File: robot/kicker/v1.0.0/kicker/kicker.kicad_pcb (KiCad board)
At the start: 2 copper layers, 0 parts

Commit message: first layout
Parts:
- added C1: 22u 25V, Capacitor_SMD:C_1210_3225Metric, F.Cu at (161.2, 130.9)
- added C10: 1000uF 200V, AT-Capacitors:ESMQ201VSN102MQ35S, F.Cu at (248.0, 177.0)
- added C11: 0.1u, Capacitor_SMD:C_0603_1608Metric, F.Cu at (427.7, 50.1)
- added C12: 0.1u, Capacitor_SMD:C_0603_1608Metric, F.Cu at (97.0, 99.5)
- added C13: 330u 50V, AT-Capacitors:WE-860160675028, F.Cu at (181.6, 164.3)
- added C14: 10u 50V, Capacitor_SMD:C_1210_3225Metric, F.Cu at (209.8, 175.6)
- added C15: 10u 35V, Capacitor_SMD:C_1206_3216Metric, B.Cu at (217.9, 129.9)
- added C16: 0.1u, Capacitor_SMD:C_0603_1608Metric, F.Cu at (371.4, 123.2)
- added C17: 10u 50V, Capacitor_SMD:C_1210_3225Metric, F.Cu at (213.3, 175.6)
- added C18: 0.1u, Capacitor_SMD:C_0603_1608Metric, F.Cu at (363.4, 126.1)
- added C19: 0.1u, Capacitor_SMD:C_0603_1608Metric, F.Cu at (218.0, 128.5)
- added C2: 47u 10V, Capacitor_SMD:C_1210_3225Metric, F.Cu at (77.6, 108.1)
- added C20: 10u 50V, Capacitor_SMD:C_1210_3225Metric, F.Cu at (216.8, 175.6)
- added C21: 10u 50V, Capacitor_SMD:C_1210_3225Metric, F.Cu at (220.3, 175.6)
- added C22: 0.1u 200V, Capacitor_SMD:C_1206_3216Metric, F.Cu at (208.9, 130.1)
- added C23: 10u 50v, Capacitor_SMD:C_1210_3225Metric, F.Cu at (449.5, 77.2)
- added C24: 0.1u, Capacitor_SMD:C_0603_1608Metric, F.Cu at (470.4, 71.1)
- added C25: DNP, Capacitor_SMD:C_0603_1608Metric, F.Cu at (470.4, 68.6)
- added C26: DNP, Capacitor_SMD:C_0603_1608Metric, F.Cu at (462.4, 76.3)
- added C27: 4u7 25V, Capacitor_SMD:C_0805_2012Metric, F.Cu at (119.1, 54.1)
- added C28: 0.1u, Capacitor_SMD:C_0603_1608Metric, F.Cu at (105.0, 71.9)
- added C29: 0.1u, Capacitor_SMD:C_0603_1608Metric, F.Cu at (111.0, 64.0)
- added C3: 1u 10V, Capacitor_SMD:C_0603_1608Metric, F.Cu at (106.4, 94.1)
- added C30: 10n 10V, Capacitor_SMD:C_0603_1608Metric, F.Cu at (126.1, 50.0)
- added C31: 1u 10V, Capacitor_SMD:C_0603_1608Metric, F.Cu at (97.0, 79.5)
- added C32: 4u7 25V, Capacitor_SMD:C_0805_2012Metric, F.Cu at (106.3, 66.6)
- added C4: 47u 10V, Capacitor_SMD:C_1210_3225Metric, F.Cu at (155.6, 130.9)
- added C5: 1u 10V, Capacitor_SMD:C_0603_1608Metric, F.Cu at (86.6, 112.3)
- added C6: 1000uF 200V, AT-Capacitors:ESMQ201VSN102MQ35S, F.Cu at (248.0, 122.8)
- added C7: 0.1u, Capacitor_SMD:C_0603_1608Metric, F.Cu at (101.0, 99.5)
- added C8: 1000uF 200V, AT-Capacitors:ESMQ201VSN102MQ35S, F.Cu at (248.0, 149.9)
- added C9: 0.1u, Capacitor_SMD:C_0603_1608Metric, F.Cu at (434.5, 41.3)
- added D1: Green, AT-LED:LED0603, F.Cu at (69.8, 112.0)
- added D10: FR3G_R1_00001, Diode_SMD:D_SMC, F.Cu at (237.0, 112.0)
- added D11: FR3G_R1_00001, Diode_SMD:D_SMC, F.Cu at (237.7, 187.3)
- added D12: Blue, AT-LED:LED0603, F.Cu at (111.0, 61.5)
- added D13: Green, AT-LED:LED0603, F.Cu at (130.3, 42.5)
- added D14: Red, AT-LED:LED0603, F.Cu at (97.0, 77.0)
- added D2: MURS460, Diode_SMD:D_SMC, F.Cu at (91.0, 94.2)
- added D3: Green, AT-LED:LED0603, F.Cu at (78.5, 111.5)
- added D4: 824521261, AT-Discrete:D_SMB_Non-Polar, F.Cu at (148.6, 131.3)
- added D5: MURS460, Diode_SMD:D_SMC, F.Cu at (427.1, 41.4)
- added D6: Green, AT-LED:LED0603, F.Cu at (82.6, 110.8)
- added D7: 824540121, Diode_SMD:D_SMC, F.Cu at (79.2, 91.7)
- added D8: RED, AT-LED:LED0603, F.Cu at (434.5, 38.8)
- added D9: MURS460, Diode_SMD:D_SMC, F.Cu at (236.5, 167.5)
- added F1: 40A, AT-Fuses:3557-2, F.Cu at (199.2, 171.5)
- added F2: 1.5A Fast Blow, Fuse:Fuse_0603_1608Metric, F.Cu at (106.4, 91.5)
- added F3: 1.5A Fast Blow, Fuse:Fuse_0603_1608Metric, F.Cu at (90.8, 107.2)
- added H1: M3, MountingHole:MountingHole_3.2mm_M3, F.Cu at (182.5, 177.5)
- added H2: M3, MountingHole:MountingHole_3.2mm_M3, F.Cu at (237.5, 177.5)
- added H3: M3, MountingHole:MountingHole_3.2mm_M3, F.Cu at (182.5, 122.5)
- added H4: M3, MountingHole:MountingHole_3.2mm_M3, F.Cu at (237.5, 122.5)
- added J1: XT30PW-M, Connector_AMASS:AMASS_XT30PW-M_1x02_P2.50mm_Horizontal, F.Cu at (192.5, 184.8)
- added J2: 1054052108, AT-Connectors:1054052108, F.Cu at (195.0, 106.5)
- added J3: 2157601002, AT-Connectors:2157601002, F.Cu at (243.5, 103.0)
- added J4: 2157601002, AT-Connectors:2157601002, F.Cu at (243.7, 196.0)
- added J5: Conn_ARM_JTAG_SWD_10, AT-Connectors:Samtec-2x5pin-0.5mm, F.Cu at (99.0, 71.7)
- added J6: Conn_01x03, Connector_PinSocket_2.54mm:PinSocket_1x03_P2.54mm_Horizontal, F.Cu at (185.9, 191.5)
- added J7: Conn_01x03, Connector_PinSocket_2.54mm:PinSocket_1x03_P2.54mm_Horizontal, F.Cu at (186.4, 128.5)
- added JP1: Power Iso., Jumper:SolderJumper-2_P1.3mm_Bridged_RoundedPad1.0x1.5mm, F.Cu at (423.8, 47.0)
- added JP2: Charge Bypass Jumper, Jumper:SolderJumper-2_P1.3mm_Open_RoundedPad1.0x1.5mm, F.Cu at (74.3, 112.0)
- added JP3: Kick Bypass Jumper, Jumper:SolderJumper-2_P1.3mm_Open_RoundedPad1.0x1.5mm, F.Cu at (92.8, 99.8)
- added JP4: Chip Bypass Jumper, Jumper:SolderJumper-2_P1.3mm_Open_RoundedPad1.0x1.5mm, F.Cu at (82.6, 107.8)
- added JP5: Fault Bypass Jumper, Jumper:SolderJumper-2_P1.3mm_Open_RoundedPad1.0x1.5mm, F.Cu at (70.0, 109.0)
- added JP6: SolderJumper_2_Bridged, Jumper:SolderJumper-2_P1.3mm_Bridged_RoundedPad1.0x1.5mm, F.Cu at (215.5, 123.0)
- added JP7: Disable Micro, Jumper:SolderJumper-2_P1.3mm_Open_RoundedPad1.0x1.5mm, F.Cu at (121.9, 50.6)
- added L1: 650 @100MHz, Resistor_SMD:R_0603_1608Metric, F.Cu at (367.8, 115.7)
- added L2: 650 @100MHz, Resistor_SMD:R_0603_1608Metric, F.Cu at (371.8, 115.7)
- added L3: GA3460-BL, AT-Inductors:GA34XX-BL, F.Cu at (219.5, 152.0)
- added L4: 650 @100MHz, Resistor_SMD:R_0603_1608Metric, F.Cu at (115.0, 61.5)
- added Q1: BSC0402NSATMA1, Package_TO_SOT_SMD:TDSON-8-1, F.Cu at (213.0, 130.5)
- added Q2: IXXH110N65C4, Package_TO_SOT_THT:TO-247-3_Horizontal_TabDown, F.Cu at (229.4, 113.0)
- added Q3: IXXH110N65C4, Package_TO_SOT_THT:TO-247-3_Horizontal_TabDown, F.Cu at (230.6, 196.7)
- added Q4: BSS138K, Package_TO_SOT_SMD:SOT-23, F.Cu at (106.5, 62.9)
- added R1: 22k, Resistor_SMD:R_0603_1608Metric, F.Cu at (416.5, 62.4)
- added R10: 1M47, Resistor_SMD:R_0603_1608Metric, F.Cu at (428.0, 46.5)
- added R11: 15k, Resistor_SMD:R_0603_1608Metric, F.Cu at (97.0, 102.0)
- added R12: 100k, Resistor_SMD:R_0603_1608Metric, F.Cu at (367.4, 123.2)
- added R13: 100k, Resistor_SMD:R_0603_1608Metric, F.Cu at (375.8, 116.0)
- added R14: 100k, Resistor_SMD:R_0603_1608Metric, F.Cu at (375.4, 123.6)
- added R15: 316k 1%, Resistor_SMD:R_0603_1608Metric, F.Cu at (379.5, 121.1)
- added R16: 523k 1%, Resistor_SMD:R_0603_1608Metric, F.Cu at (371.4, 125.7)
- added R17: 205k 1%, Resistor_SMD:R_0603_1608Metric, F.Cu at (375.4, 121.1)
- added R18: 226k 1%, Resistor_SMD:R_0603_1608Metric, F.Cu at (379.8, 116.0)
- added R19: 36k5 1%, Resistor_SMD:R_0603_1608Metric, F.Cu at (225.3, 123.1)
- added R2: 10k, Resistor_SMD:R_0603_1608Metric, F.Cu at (423.7, 52.6)
- added R20: 1 1%, Resistor_SMD:R_0603_1608Metric, F.Cu at (208.5, 126.2)
- added R21: 4k21, Resistor_SMD:R_0603_1608Metric, F.Cu at (218.0, 130.0)
- added R22: 36k5 1%, Resistor_SMD:R_0603_1608Metric, F.Cu at (222.0, 132.5)
- added R23: 80k6 1%, Resistor_SMD:R_0603_1608Metric, F.Cu at (220.5, 132.5)
- added R24: 3m00 1% 1W, AT-Resistors:1206-CS, F.Cu at (214.2, 125.5)
- added R25: 237k 1%, Resistor_SMD:R_0603_1608Metric, B.Cu at (230.5, 126.0)
- added R26: 237k 1%, Resistor_SMD:R_0603_1608Metric, B.Cu at (230.5, 122.5)
- added R27: 2k94 1%, Resistor_SMD:R_0603_1608Metric, B.Cu at (230.5, 118.0)
- added R28: 100k, Resistor_SMD:R_0603_1608Metric, F.Cu at (454.4, 76.3)
- added R29: 100k, Resistor_SMD:R_0603_1608Metric, F.Cu at (474.4, 68.6)
- added R3: 267k, Resistor_SMD:R_0603_1608Metric, F.Cu at (438.6, 38.8)
- added R30: 100k, Resistor_SMD:R_0603_1608Metric, F.Cu at (458.4, 76.3)
- added R31: 100k, Resistor_SMD:R_0603_1608Metric, F.Cu at (483.6, 58.1)
- added R32: 10, Resistor_SMD:R_0603_1608Metric, F.Cu at (483.6, 55.6)
- added R33: 10, Resistor_SMD:R_0603_1608Metric, F.Cu at (492.1, 49.1)
- added R34: 100k, Resistor_SMD:R_0603_1608Metric, F.Cu at (118.9, 56.9)
- added R35: 10k, Resistor_SMD:R_0603_1608Metric, F.Cu at (105.0, 69.3)
- added R36: 10k, Resistor_SMD:R_0603_1608Metric, F.Cu at (130.3, 45.0)
- added R37: 10k, Resistor_SMD:R_0603_1608Metric, F.Cu at (123.4, 53.6)
- added R4: 18k7, Resistor_SMD:R_0603_1608Metric, F.Cu at (92.6, 102.8)
- added R5: 10k, Resistor_SMD:R_0603_1608Metric, F.Cu at (408.5, 70.3)
- added R6: 510k, Resistor_SMD:R_0603_1608Metric, F.Cu at (86.7, 107.2)
- added R7: 510k, Resistor_SMD:R_0603_1608Metric, F.Cu at (86.7, 109.8)
- added R8: 15k, Resistor_SMD:R_0603_1608Metric, F.Cu at (432.0, 46.5)
- added R9: 1M47, Resistor_SMD:R_0603_1608Metric, F.Cu at (423.7, 50.1)
- added SW1: TS02-66-73-BK-160-SCR-D, at-switches:TS02-66-73-BK-160-SCR-D, F.Cu at (99.6, 64.2)
- added TP1: ~{DONE}, TestPoint:TestPoint_Pad_D1.5mm, F.Cu at (375.1, 128.8)
- added TP2: CHG_EN, TestPoint:TestPoint_Pad_D1.5mm, F.Cu at (363.2, 134.8)
- added TP3: ~{FAULT}, TestPoint:TestPoint_Pad_D1.5mm, F.Cu at (366.7, 134.8)
- added TP5: SPICE: V_{drain} <<<HIGH VOLTAGE>>>, TestPoint:TestPoint_Pad_D1.0mm, F.Cu at (209.0, 133.5)
- added TP6: SPICE: V_{out} <<<HIGH VOLTAGE>>>, TestPoint:TestPoint_Pad_D1.5mm, F.Cu at (240.2, 162.0)
- added TP7: FB, TestPoint:TestPoint_Pad_D1.5mm, B.Cu at (229.0, 130.5)
- added U1: LM1117-5.0, Package_TO_SOT_SMD:TO-252-2, F.Cu at (150.5, 124.5)
- added U2: LM1117-3.3, Package_TO_SOT_SMD:SOT-223-3_TabPin2, F.Cu at (161.5, 124.7)
- added U3: ADUM7441, Package_SO:QSOP-16_3.9x4.9mm_P0.635mm, F.Cu at (195.0, 126.0)
- added U4: LT3751-QFN, AT-IC:LT3751-QFN20_EP_4x5mm_P0.5mm, F.Cu at (220.5, 125.0)
- added U5: IX4427, Package_SO:SOIC-8_3.9x4.9mm_P1.27mm, F.Cu at (485.8, 51.1)
- added U6: STM32F030K6Tx, Package_QFP:LQFP-32_7x7mm_P0.8mm, F.Cu at (114.1, 46.9)
- added U7: SK9822, AT-LED:SK9822, F.Cu at (124.0, 45.0)
- added U8: SK9822, AT-LED:SK9822, F.Cu at (112.6, 56.4)
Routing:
- net +BATT: track 0.00 -> 62.1 mm, vias 0 -> 30
- net /flyback_charger/FB: track 0.00 -> 28.7 mm, vias 0 -> 1
- net /flyback_charger/HVGATE: track 0.00 -> 16.4 mm, vias 0 -> 2
- net /flyback_charger/V_{solenoid}: track 0.00 -> 15.5 mm, vias 0 -> 1
- net GND: track 0.00 -> 10.5 mm, vias 0 -> 92
- net /flyback_charger/RDCM: track 0.00 -> 7.28 mm
- net +12V: track 0.00 -> 6.56 mm, vias 0 -> 1
- net /flyback_charger/RV_{out}: track 0.00 -> 5.29 mm
- net /flyback_charger/UVLO1: track 0.00 -> 4.97 mm, vias 0 -> 1
- net /flyback_charger/RBG: track 0.00 -> 4.29 mm
- net /flyback_charger/V_{trans}: track 0.00 -> 4.11 mm
- net /CMD_{CHG}: track 0.00 -> 3.54 mm, vias 0 -> 1
- net /STATUS_{~{FAULT}}: track 0.00 -> 3.11 mm, vias 0 -> 1
- net /STATUS_{~{DONE}}: track 0.00 -> 3.10 mm, vias 0 -> 1
- net /flyback_charger/RV_{trans}: track 0.00 -> 3.08 mm
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- added copper zone on B.Cu, net +BATT
- added copper zone on F.Cu, net +BATT
- added copper zone on In1.Cu, net +BATT
- added copper zone on In2.Cu, net +BATT
- added copper zone on B.Cu, net +V_{BATT(RAW)}
- added copper zone on F.Cu, net +V_{BATT(RAW)}
- added copper zone on In1.Cu, net +V_{BATT(RAW)}
- added copper zone on In2.Cu, net +V_{BATT(RAW)}
- added copper zone on F.Cu, net /flyback_charger/HV_AC
- added copper zone on F.Cu, net /flyback_charger/V_{solenoid}
- added copper zone on F.Cu, net /flyback_charger/V_{trans}
- added copper zone on F.Cu, net /flyback_charger/V_{trans}_SOURCE
- added copper zone on B.Cu, net GND
- added copper zone on F.Cu, net GND
- added copper zone on In1.Cu, net GND
- added copper zone on In2.Cu, net GND
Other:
- board outline added: 73 x 110 mm
- copper layers 2 -> 4
- board text added: "BATTERY"

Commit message: significant 3751 layout improvements
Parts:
- added C23: 0.1u 500V, Capacitor_SMD:C_1210_3225Metric, F.Cu at (211.8, 131.4)
- added C24: 0.47u 500V, Capacitor_SMD:C_2225_5664Metric, F.Cu at (225.8, 130.2)
- added C25: 0.47u 500V, Capacitor_SMD:C_2225_5664Metric, F.Cu at (217.3, 130.2)
- C15, R25, R26, R27: moved to F.Cu
- JP6: value SolderJumper_2_Bridged -> CCM_EN
- Q2, Q3: moved to B.Cu
- R20: footprint Resistor_SMD:R_0603_1608Metric -> Resistor_SMD:R_0805_2012Metric
- moved J4 97.0 mm to (192.6, 113.6), turned to 180 degrees
- moved J2 92.9 mm to (149.2, 187.3), turned to 0 degrees
- moved Q3 85.2 mm to (215.8, 112.7), turned to 0 degrees
- moved D11 67.6 mm to (224.4, 121.0), turned to 180 degrees
- moved TP6 67.0 mm to (290.6, 104.2)
- moved D9 52.3 mm to (200.0, 130.0)
- moved U3 52.2 mm to (146.9, 146.2)
- moved R27 51.1 mm to (233.0, 169.0), turned to 90 degrees
- moved JP6 48.4 mm to (230.6, 169.0), turned to 90 degrees
- moved R26 42.6 mm to (233.0, 165.0), turned to 90 degrees
- moved U4 42.0 mm to (216.3, 166.8), turned to 90 degrees
- moved R24 41.7 mm to (222.6, 166.3), turned to 0 degrees
- moved R19 40.9 mm to (212.2, 161.9)
- moved C15 40.8 mm to (208.8, 169.7)
- moved D10 36.7 mm to (201.4, 121.0), turned to 0 degrees
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- renumbered C23 to C26, C24 to C27, C25 to C28, C26 to C29, C27 to C30, C28 to C31, C29 to C32, C30 to C33, C31 to C34, C32 to C35, TP5 to TP4, TP6 to TP5, TP7 to TP6
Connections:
- L3 pad 1: +BATT -> /flyback_charger/V_{trans}
- L3 pad 10: /flyback_charger/V_{trans} -> +BATT
- L3 pad 11: /flyback_charger/V_{trans} -> +BATT
- L3 pad 12: /flyback_charger/V_{trans} -> +BATT
- L3 pad 2: +BATT -> /flyback_charger/V_{trans}
- L3 pad 3: +BATT -> /flyback_charger/V_{trans}
- L3 pad 4: +BATT -> /flyback_charger/V_{trans}
- L3 pad 6: /flyback_charger/HV_AC -> GND
- L3 pad 7: GND -> /flyback_charger/HV_AC
- L3 pad 9: /flyback_charger/V_{trans} -> +BATT
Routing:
- net +BATT: track 62.1 -> 14.5 mm, vias 30 -> 0
- net /flyback_charger/V_{solenoid}: track 15.5 -> 52.4 mm, vias 1 -> 54
- net /flyback_charger/V_{trans}: track 4.11 -> 13.0 mm
- net GND: track 10.5 -> 18.7 mm, vias 92 -> 104
- net /flyback_charger/FB: track 28.7 -> 25.4 mm, vias 1 -> 0
- net /flyback_charger/RV_{out}: track 5.29 -> 2.29 mm
- net /flyback_charger/RDCM: track 7.28 -> 4.40 mm
- net /flyback_charger/RV_{trans}: track 3.08 -> 5.70 mm
- net /solenoid_control/GATE_{kick}_FILT: track 0.00 -> 1.85 mm
- net /flyback_charger/HVGATE: track 16.4 -> 14.8 mm
- net +12V: track 6.56 -> 5.23 mm
- added copper zone on In1.Cu, net /flyback_charger/V_{solenoid}
- removed copper zone on B.Cu, net +BATT
- removed copper zone on F.Cu, net +BATT
- removed copper zone on In1.Cu, net +BATT
- removed copper zone on In2.Cu, net +BATT

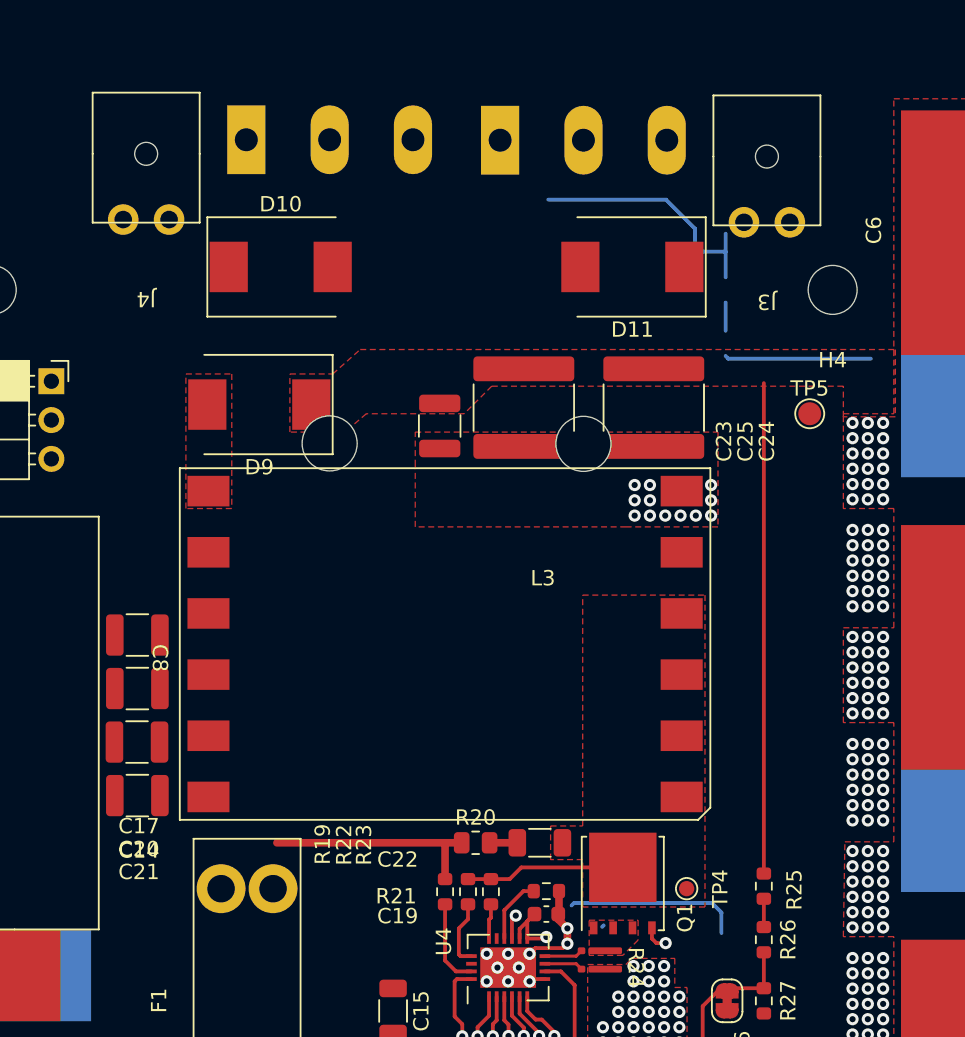
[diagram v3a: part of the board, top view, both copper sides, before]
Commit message: update IGBT choice
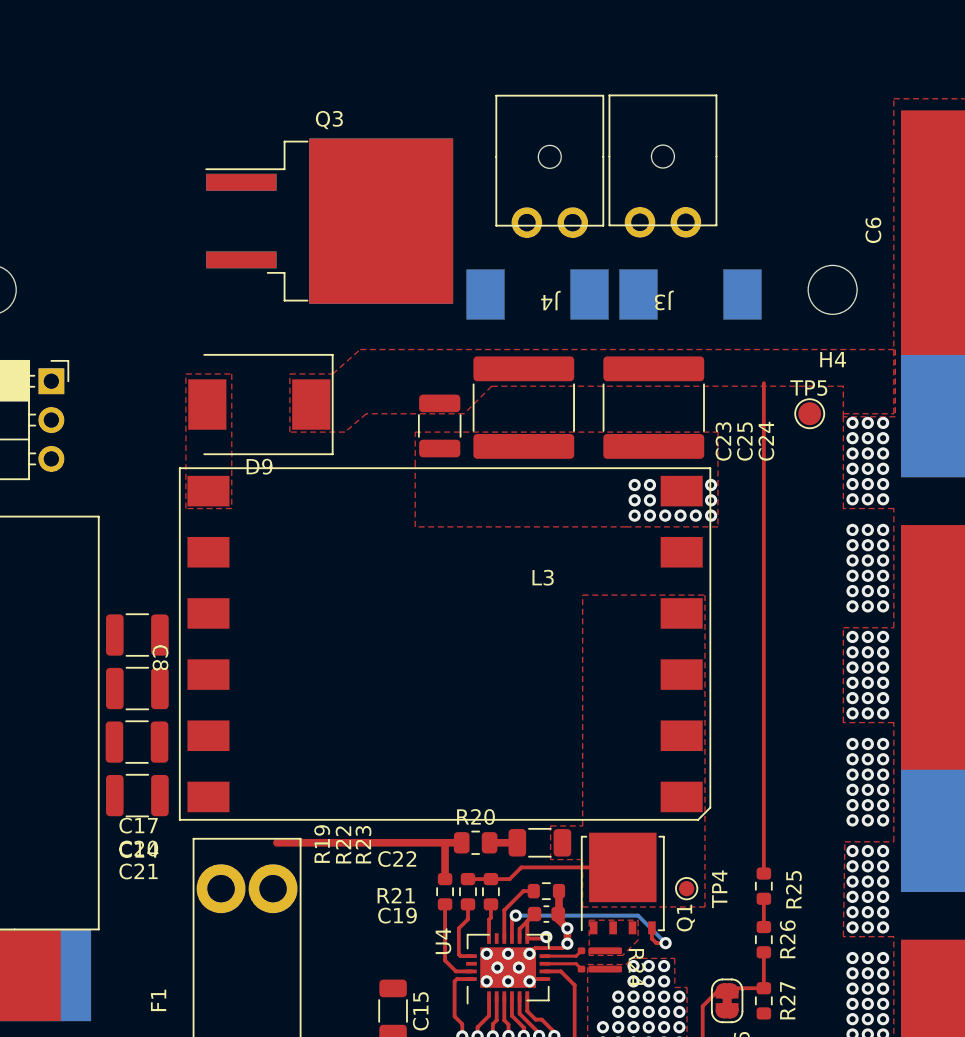
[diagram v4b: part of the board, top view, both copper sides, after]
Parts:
- D10, D11: moved to B.Cu
- Q2: value IXXH110N65C4 -> IXGA48N60A3; footprint Package_TO_SOT_THT:TO-247-3_Horizontal_TabDown -> Package_TO_SOT_SMD:TO-263-2
- Q3: value IXXH110N65C4 -> IXGA48N60A3; footprint Package_TO_SOT_THT:TO-247-3_Horizontal_TabDown -> Package_TO_SOT_SMD:TO-263-2; moved to F.Cu
- moved D10 26.9 mm to (228.2, 122.8)
- moved J4 26.4 mm to (219.0, 113.8)
- moved Q3 12.3 mm to (204.6, 118.0)
- moved Q2 7.62 mm to (204.6, 118.0)
- moved J3 6.80 mm to (226.4, 113.8)
- moved D11 6.46 mm to (218.2, 122.8), turned to 0 degrees
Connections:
- U6 pad 25: unconnected-(U6-Pad25) -> /BOOT0
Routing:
- net /flyback_charger/V_{solenoid}: track 52.4 -> 36.0 mm
- net GND: track 18.7 -> 9.17 mm
- net /solenoid_control/GATE_{kick}_FILT: track 1.85 -> 0.00 mm
- net /flyback_charger/HVGATE: track 14.8 -> 13.9 mm

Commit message: layout work
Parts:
- C1, C16, C18, C4, D4, L1, L2, R15, R16, R17, R18, U1, U2: moved to B.Cu
- J2: footprint AT-Connectors:1054052108 -> Connector_JST:JST_SH_BM08B-SRSS-TB_1x08-1MP_P1.00mm_Vertical
- J6, J7: footprint Connector_PinSocket_2.54mm:PinSocket_1x03_P2.54mm_Horizontal -> Connector_JST:JST_SH_SM03B-SRSS-TB_1x03-1MP_P1.00mm_Horizontal
- Q2, Q3: footprint Package_TO_SOT_SMD:TO-263-2 -> Package_TO_SOT_SMD:TO-268-2
- moved SW1 182.9 mm to (230.8, 191.6)
- moved U7 176.2 mm to (221.8, 191.6)
- moved R15 176.0 mm to (210.8, 171.3)
- moved R18 173.3 mm to (216.3, 173.6), turned to 90 degrees
- moved J5 172.5 mm to (230.6, 183.2)
- moved U6 171.7 mm to (221.4, 181.0)
- moved C16 171.1 mm to (207.7, 172.9), turned to 180 degrees
- moved L1 169.5 mm to (207.7, 171.3)
- moved R17 169.1 mm to (214.7, 173.6), turned to 90 degrees
- moved R16 167.4 mm to (210.8, 172.9)
- moved L2 166.0 mm to (217.1, 176.0), turned to 180 degrees
- moved C18 157.6 mm to (213.9, 176.0), turned to 180 degrees
- moved U8 130.1 mm to (179.8, 167.8)
- moved U1 88.8 mm to (210.3, 190.2)
- moved U2 88.6 mm to (221.3, 190.1)
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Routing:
- net +12V: track 5.09 -> 16.6 mm
- net /CMD_{CHG}: track 3.54 -> 11.4 mm, vias 1 -> 0
- net /STATUS_{~{DONE}}: track 3.10 -> 10.9 mm, vias 1 -> 0
- net /STATUS_{~{FAULT}}: track 3.11 -> 10.8 mm, vias 1 -> 0
- net /flyback_charger/V_{cc}_FILT: track 0.00 -> 4.79 mm
- net /flyback_charger/V_{batt}_FILT: track 0.00 -> 4.72 mm
- net /flyback_charger/OVLO1: track 2.91 -> 6.33 mm
- net /flyback_charger/UVLO2: track 2.70 -> 4.39 mm
- net /flyback_charger/UVLO1: track 4.97 -> 6.63 mm
- net /flyback_charger/OVLO2: track 2.69 -> 4.16 mm
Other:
- board size 73 x 110 mm -> 73 x 90 mm
- board text added: "CHIP"
- board text added: "KICK"

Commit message: kicker routing progress
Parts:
- removed the C28 at (470.4, 68.6)
- removed the C29 at (462.4, 76.3)
- removed the JP2 at (74.3, 112.0)
- removed the JP3 at (92.8, 99.8)
- removed JP4: Chip Bypass Jumper, Jumper:SolderJumper-2_P1.3mm_Open_RoundedPad1.0x1.5mm
- removed JP5: Fault Bypass Jumper, Jumper:SolderJumper-2_P1.3mm_Open_RoundedPad1.0x1.5mm
- added C14: 220u 50V, Capacitor_THT:CP_Radial_D10.0mm_P5.00mm, F.Cu at (187.4, 141.0)
- added D8: RED, AT-LED:LED0603, F.Cu at (248.5, 193.0)
- added R10: 1M47, Resistor_SMD:R_0603_1608Metric, F.Cu at (240.0, 184.6)
- added R11: 1M47, Resistor_SMD:R_0603_1608Metric, F.Cu at (240.0, 188.0)
- added R12: 1M47, Resistor_SMD:R_0603_1608Metric, F.Cu at (248.1, 90.9)
- added R13: 1M47, Resistor_SMD:R_0603_1608Metric, F.Cu at (244.0, 96.0)
- added R26: 100k 1%, Resistor_SMD:R_0603_1608Metric, F.Cu at (230.8, 164.6)
- added R29: 10 1%, Resistor_SMD:R_0603_1608Metric, F.Cu at (228.4, 165.4)
- added R41: 100k, Resistor_SMD:R_0603_1608Metric, F.Cu at (330.2, 168.1)
- added R9: DNP, Resistor_SMD:R_0603_1608Metric, F.Cu at (205.2, 176.0)
- added TP7: D_TEST_1, TestPoint:TestPoint_Pad_D1.5mm, F.Cu at (334.0, 168.6)
- added TP8: D_TEST_2, TestPoint:TestPoint_Pad_D1.5mm, F.Cu at (330.0, 171.1)
- C13: value 330u 50V -> 220u 50V; footprint AT-Capacitors:WE-860160675028 -> Capacitor_THT:CP_Radial_D10.0mm_P5.00mm
- C2, C3, C5, JP1: moved to B.Cu
- D11: renamed from D10; value FR3G_R1_00001 -> MURS460; moved to F.Cu
- D12: renamed from D11; value FR3G_R1_00001 -> MURS460; moved to F.Cu
- D15: renamed from D14; value Red -> Yellow
- D2, D5: value MURS460 -> CUS10S30,H3F; footprint Diode_SMD:D_SMC -> Diode_SMD:D_SOD-323; moved to B.Cu
- D7: value 824540121 -> SMF12CA; footprint Diode_SMD:D_SMC -> Diode_SMD:D_SOD-123F; moved to B.Cu
- Q2: footprint Package_TO_SOT_SMD:TO-268-2 -> Package_TO_SOT_SMD:TO-263-2
- Q3: footprint Package_TO_SOT_SMD:TO-268-2 -> Package_TO_SOT_SMD:TO-263-2; moved to B.Cu
- R6, R7: value 510k -> DNP
- R8: value 15k -> DNP
- moved R38 315.4 mm to (170.7, 97.9)
- moved R39 315.4 mm to (170.7, 95.4)
- moved R40 315.4 mm to (179.2, 88.9)
- moved R36 305.6 mm to (170.6, 101.5)
- moved U5 281.4 mm to (208.2, 97.2)
- moved C28 279.9 mm to (191.4, 93.5), turned to 90 degrees
- moved C10 279.2 mm to (209.0, 206.0)
- moved R37 278.2 mm to (181.1, 99.5)
- moved R35 273.7 mm to (182.0, 103.0), turned to 180 degrees
- moved C11 272.5 mm to (204.5, 206.5)
- moved R3 266.7 mm to (203.0, 163.8), turned to -90 degrees
- moved R8 262.6 mm to (203.6, 176.0), turned to 90 degrees
- moved D5 258.3 mm to (224.0, 201.0), turned to 180 degrees
- moved JP1 252.0 mm to (217.0, 191.0), turned to 180 degrees
- moved C27 250.1 mm to (200.0, 93.5), turned to 90 degrees
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- renumbered C9 to C10, C14 to C15, C15 to C16, C16 to C17, C17 to C18, C18 to C19, C19 to C20, C20 to C21, C21 to C22, C22 to C23, C23 to C24, C24 to C25, C25 to C26, C26 to C27, C27 to C28, C30 to C29, C31 to C30, C32 to C31, C33 to C32, C34 to C33, C35 to C34, C8 to C7, C7 to C8, C10 to C9, D9 to D10, D12 to D13, D13 to D14, D8 to D9, JP6 to JP2, JP7 to JP3, R9 to R14, R10 to R15, R11 to R16, R12 to R17, R13 to R18, R14 to R19, R15 to R20, R16 to R21, R17 to R22, R18 to R23, R19 to R24, R20 to R25, R22 to R27, R23 to R28, R21 to R30, R24 to R31, R25 to R32, R26 to R33, R27 to R34, R28 to R35, R29 to R36, R30 to R37, R31 to R38, R32 to R39, R33 to R40, R34 to R42, R35 to R43, R36 to R44, R37 to R45
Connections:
- net Net-(R10-Pad1) renamed /HVMS
- net Net-(R25-Pad1) renamed /flyback_charger/HVFBS
- D11 pad 2: Net-(D10-Pad2) -> /solenoid_control/KICK_SW
- D12 pad 2: Net-(D11-Pad2) -> /solenoid_control/CHIP_SW
- D9 pad 1: Net-(D8-Pad1) -> GND
- D9 pad 2: Net-(D8-Pad2) -> Net-(D9-Pad2)
- J3 pad 1: /flyback_charger/V_{solenoid} -> /solenoid_control/KICK_SW
- J3 pad 2: Net-(D10-Pad2) -> /flyback_charger/V_{solenoid}
- J4 pad 1: /flyback_charger/V_{solenoid} -> /solenoid_control/CHIP_SW
- J4 pad 2: Net-(D11-Pad2) -> /flyback_charger/V_{solenoid}
- Q1 pad 4: /flyback_charger/HVGATE -> Net-(Q1-Pad4)
- Q2 pad 2: Net-(D10-Pad2) -> /solenoid_control/KICK_SW
- Q3 pad 2: Net-(D11-Pad2) -> /solenoid_control/CHIP_SW
- R6 pad 1: /flyback_charger/V_{solenoid} -> /RST_CHG_PROT
- R6 pad 2: Net-(R6-Pad2) -> /CMD_{CHG}
- R7 pad 1: Net-(R6-Pad2) -> /BOOT0_KICK_PROT
- R7 pad 2: Net-(D8-Pad2) -> /CMD_{kick}
- R8 pad 1: Net-(D8-Pad1) -> /RX_CHIP_PROT
- R8 pad 2: GND -> /CMD_{chip}
- U6 pad 29: unconnected-(U6-Pad29) -> Net-(TP7-Pad1)
- U6 pad 30: unconnected-(U6-Pad30) -> Net-(TP8-Pad1)
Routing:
- net /RST_CHG_PROT: track 0.00 -> 19.3 mm
- net /BOOT0_KICK_PROT: track 0.00 -> 18.7 mm
- net /RX_CHIP_PROT: track 0.00 -> 18.1 mm
- net /TX_FAULT_PROT: track 0.00 -> 17.7 mm
- net /digital/DOTSTAR_SCK: track 0.00 -> 14.4 mm
- net VBUS: track 0.00 -> 14.1 mm
- net /digital/DOTSTAR_MOSI: track 0.00 -> 13.9 mm
- net GND: track 9.17 -> 21.5 mm, vias 104 -> 111
- net /CMD_{CHG}: track 11.4 -> 2.75 mm
- net /STATUS_{~{DONE}}: track 10.9 -> 2.92 mm
- net /STATUS_{~{FAULT}}: track 10.8 -> 3.05 mm
- net /12V0_UNPROT: track 0.00 -> 5.89 mm
- net Net-(D7-Pad2): track 0.00 -> 5.15 mm, vias 0 -> 1
- net /flyback_charger/HVGATE: track 13.9 -> 17.6 mm
- net +5V: track 0.00 -> 3.01 mm, vias 0 -> 1
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- removed copper zone on B.Cu, net +V_{BATT(RAW)}
- removed copper zone on In2.Cu, net +V_{BATT(RAW)}
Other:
- board size 73 x 90 mm -> 76 x 90 mm
